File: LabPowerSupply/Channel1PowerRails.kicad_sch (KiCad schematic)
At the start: 8 parts

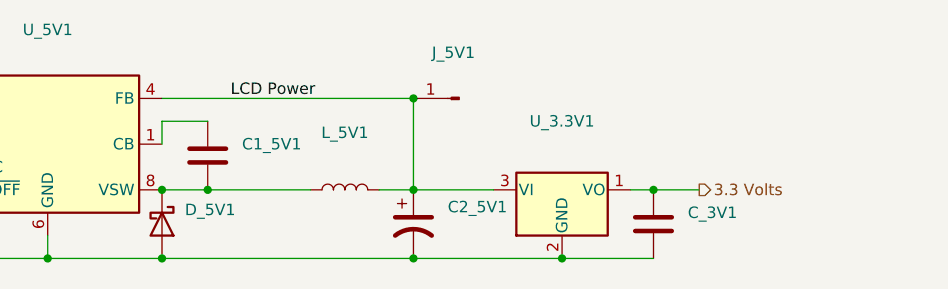
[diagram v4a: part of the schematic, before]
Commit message: Changed capacitor footprints, added resistor and diode to linear
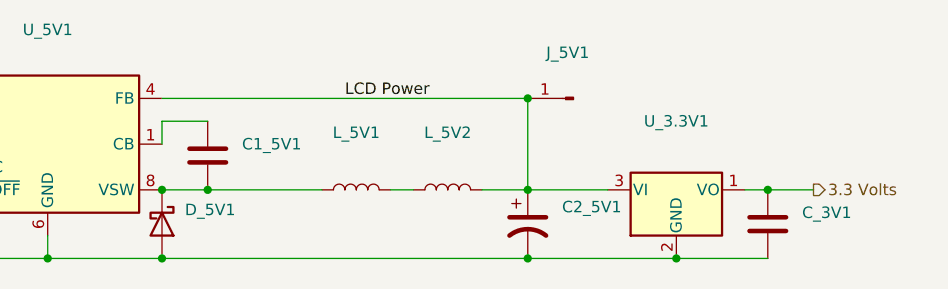
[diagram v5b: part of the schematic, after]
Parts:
- added L_5V1: (no value), symbol Device:L
- renumbered L_5V1 to L_5V2
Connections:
- net at C1_5V1.2, D_5V1.1 (K), U_5V1.8 (VSW): now also L_5V1.1; no longer L_5V2.1
- new net: L_5V1.2, L_5V2.1
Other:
- moved on the sheet: C2_5V1, C_3V1, J_5V1, L_5V2, U_3.3V1
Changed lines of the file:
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@@
   (junction (at 139.7 99.06) (diameter 0) (color 0 0 0 0)
+  )
+  (junction (at 144.78 99.06) (diameter 0) (color 0 0 0 0)
   )
   (junction (at 139.7 106.68) (diameter 0) (color 0 0 0 0)
   )
-  (junction (at 144.78 99.06) (diameter 0) (color 0 0 0 0)
+  (junction (at 180.34 99.06) (diameter 0) (color 0 0 0 0)
   )
-  (junction (at 167.64 99.06) (diameter 0) (color 0 0 0 0)
+  (junction (at 180.34 88.9) (diameter 0) (color 0 0 0 0)
   )
-  (junction (at 167.64 88.9) (diameter 0) (color 0 0 0 0)
+  (junction (at 207.01 99.06) (diameter 0) (color 0 0 0 0)
   )
-  (junction (at 194.31 99.06) (diameter 0) (color 0 0 0 0)
+  (junction (at 180.34 106.68) (diameter 0) (color 0 0 0 0)
   )
-  (junction (at 167.64 106.68) (diameter 0) (color 0 0 0 0)
-  )
-  (junction (at 184.15 106.68) (diameter 0) (color 0 0 0 0)
+  (junction (at 196.85 106.68) (diameter 0) (color 0 0 0 0)
   )
   (no_connect (at 114.3 96.52))
@@
     (stroke (width 0) (type default) (color 0 0 0 0))
   )
-  (wire (pts (xy 167.64 99.06) (xy 176.53 99.06))
+  (wire (pts (xy 180.34 99.06) (xy 189.23 99.06))
     (stroke (width 0) (type default) (color 0 0 0 0))
   )
@@
     (stroke (width 0) (type default) (color 0 0 0 0))
   )
-  (wire (pts (xy 156.21 99.06) (xy 144.78 99.06))
+  (wire (pts (xy 144.78 99.06) (xy 157.48 99.06))
+    (stroke (width 0) (type default) (color 0 0 0 0))
+  )
+  (wire (pts (xy 139.7 106.68) (xy 180.34 106.68))
     (stroke (width 0) (type default) (color 0 0 0 0))
   )
@@
     (stroke (width 0) (type default) (color 0 0 0 0))
   )
-  (wire (pts (xy 167.64 88.9) (xy 139.7 88.9))
+  (wire (pts (xy 139.7 88.9) (xy 180.34 88.9))
     (stroke (width 0) (type default) (color 0 0 0 0))
   )
-  (wire (pts (xy 167.64 106.68) (xy 184.15 106.68))
+  (wire (pts (xy 180.34 106.68) (xy 196.85 106.68))
     (stroke (width 0) (type default) (color 0 0 0 0))
   )
-  (wire (pts (xy 167.64 99.06) (xy 167.64 88.9))
+  (wire (pts (xy 180.34 99.06) (xy 180.34 88.9))
+    (stroke (width 0) (type default) (color 0 0 0 0))
+  )
+  (wire (pts (xy 165.1 99.06) (xy 167.64 99.06))
     (stroke (width 0) (type default) (color 0 0 0 0))
   )
@@
     (stroke (width 0) (type default) (color 0 0 0 0))
   )
-  (wire (pts (xy 139.7 106.68) (xy 167.64 106.68))
-    (stroke (width 0) (type default) (color 0 0 0 0))
-  )
   (wire (pts (xy 113.03 106.68) (xy 127 106.68))
     (stroke (width 0) (type default) (color 0 0 0 0))
   )
-  (wire (pts (xy 184.15 106.68) (xy 194.31 106.68))
+  (wire (pts (xy 196.85 106.68) (xy 207.01 106.68))
     (stroke (width 0) (type default) (color 0 0 0 0))
   )
-  (wire (pts (xy 194.31 99.06) (xy 199.39 99.06))
+  (wire (pts (xy 207.01 99.06) (xy 212.09 99.06))
     (stroke (width 0) (type default) (color 0 0 0 0))
   )
-  (wire (pts (xy 191.77 99.06) (xy 194.31 99.06))
+  (wire (pts (xy 204.47 99.06) (xy 207.01 99.06))
     (stroke (width 0) (type default) (color 0 0 0 0))
   )
-  (wire (pts (xy 163.83 99.06) (xy 167.64 99.06))
+  (wire (pts (xy 175.26 99.06) (xy 180.34 99.06))
     (stroke (width 0) (type default) (color 0 0 0 0))
   )
-  (label "LCD Power" (at 147.32 88.9 0)
+  (label "LCD Power" (at 160.02 88.9 0)
     (effects (font (size 1.27 1.27)) (justify left bottom))
   )
@@
     (effects (font (size 1.27 1.27)) (justify right))
   )
-  (hierarchical_label "3.3 Volts" (shape output) (at 199.39 99.06 0)
+  (hierarchical_label "3.3 Volts" (shape output) (at 212.09 99.06 0)
     (effects (font (size 1.27 1.27)) (justify left))
   )
@@
     (effects (font (size 1.27 1.27)) (justify right))
   )
-  (symbol (lib_id "Connector:Conn_01x01_Male") (at 172.72 88.9 180) (unit 1)
+  (symbol (lib_id "Connector:Conn_01x01_Male") (at 185.42 88.9 180) (unit 1)
     (in_bom yes) (on_board yes) (fields_autoplaced)
-    (property "Reference" "J_5V1" (id 0) (at 172.085 83.82 0))
-    (property "Value" "" (id 1) (at 172.085 86.36 0))
-    (property "Footprint" "" (id 2) (at 172.72 88.9 0)
+    (property "Reference" "J_5V1" (id 0) (at 184.785 83.82 0))
+    (property "Value" "" (id 1) (at 184.785 86.36 0))
+    (property "Footprint" "" (id 2) (at 185.42 88.9 0)
       (effects (font (size 1.27 1.27)) hide)
     )
-    (property "Datasheet" "~" (id 3) (at 172.72 88.9 0)
+    (property "Datasheet" "~" (id 3) (at 185.42 88.9 0)
       (effects (font (size 1.27 1.27)) hide)
     )
     (pin "1")
   )
-  (symbol (lib_id "Device:C") (at 194.31 102.87 0) (unit 1)
+  (symbol (lib_id "Device:C") (at 207.01 102.87 0) (unit 1)
     (in_bom yes) (on_board yes) (fields_autoplaced)
-    (property "Reference" "C_3V1" (id 0) (at 198.12 101.5999 0)
+    (property "Reference" "C_3V1" (id 0) (at 210.82 101.5999 0)
       (effects (font (size 1.27 1.27)) (justify left))
     )
-    (property "Value" "" (id 1) (at 198.12 104.1399 0)
+    (property "Value" "" (id 1) (at 210.82 104.1399 0)
       (effects (font (size 1.27 1.27)) (justify left))
     )
-    (property "Footprint" "" (id 2) (at 195.2752 106.68 0)
+    (property "Footprint" "" (id 2) (at 207.9752 106.68 0)
       (effects (font (size 1.27 1.27)) hide)
     )
-    (property "Datasheet" "~" (id 3) (at 194.31 102.87 0)
+    (property "Datasheet" "~" (id 3) (at 207.01 102.87 0)
       (effects (font (size 1.27 1.27)) hide)
     )
@@
     (pin "2")
   )
-  (symbol (lib_id "Regulator_Linear:LP2950-3.3_TO92") (at 184.15 99.06 0) (unit 1)
+  (symbol (lib_id "Regulator_Linear:LP2950-3.3_TO92") (at 196.85 99.06 0) (unit 1)
     (in_bom yes) (on_board yes) (fields_autoplaced)
-    (property "Reference" "U_3.3V1" (id 0) (at 184.15 91.44 0))
-    (property "Value" "" (id 1) (at 184.15 93.98 0))
-    (property "Footprint" "" (id 2) (at 184.15 93.345 0)
+    (property "Reference" "U_3.3V1" (id 0) (at 196.85 91.44 0))
+    (property "Value" "" (id 1) (at 196.85 93.98 0))
+    (property "Footprint" "" (id 2) (at 196.85 93.345 0)
       (effects (font (size 1.27 1.27) italic) hide)
     )
-    (property "Datasheet" "http://www.ti.com/lit/ds/symlink/lp2950.pdf" (id 3) (at 184.15 100.33 0)
+    (property "Datasheet" "http://www.ti.com/lit/ds/symlink/lp2950.pdf" (id 3) (at 196.85 100.33 0)
       (effects (font (size 1.27 1.27)) hide)
     )
@@
     (pin "3")
   )
-  (symbol (lib_id "Device:C_Polarized_US") (at 167.64 102.87 0) (unit 1)
+  (symbol (lib_id "Device:C_Polarized_US") (at 180.34 102.87 0) (unit 1)
     (in_bom yes) (on_board yes) (fields_autoplaced)
-    (property "Reference" "C2_5V1" (id 0) (at 171.45 100.9649 0)
+    (property "Reference" "C2_5V1" (id 0) (at 184.15 100.9649 0)
       (effects (font (size 1.27 1.27)) (justify left))
     )
-    (property "Value" "" (id 1) (at 171.45 103.5049 0)
+    (property "Value" "" (id 1) (at 184.15 103.5049 0)
       (effects (font (size 1.27 1.27)) (justify left))
     )
-    (property "Footprint" "" (id 2) (at 167.64 102.87 0)
+    (property "Footprint" "" (id 2) (at 180.34 102.87 0)
       (effects (font (size 1.27 1.27)) hide)
     )
-    (property "Datasheet" "~" (id 3) (at 167.64 102.87 0)
+    (property "Datasheet" "~" (id 3) (at 180.34 102.87 0)
       (effects (font (size 1.27 1.27)) hide)
     )
@@
     (pin "2")
   )
-  (symbol (lib_id "Device:L") (at 160.02 99.06 90) (unit 1)
+  (symbol (lib_id "Device:L") (at 161.29 99.06 90) (unit 1)
     (in_bom yes) (on_board yes) (fields_autoplaced)
-    (property "Reference" "L_5V1" (id 0) (at 160.02 92.71 90))
-    (property "Value" "" (id 1) (at 160.02 95.25 90))
-    (property "Footprint" "" (id 2) (at 160.02 99.06 0)
+    (property "Reference" "L_5V1" (id 0) (at 161.29 92.71 90))
+    (property "Value" "" (id 1) (at 161.29 95.25 90))
+    (property "Footprint" "" (id 2) (at 161.29 99.06 0)
       (effects (font (size 1.27 1.27)) hide)
     )
-    (property "Datasheet" "~" (id 3) (at 160.02 99.06 0)
+    (property "Datasheet" "~" (id 3) (at 161.29 99.06 0)
       (effects (font (size 1.27 1.27)) hide)
     )
+    (pin "1")
+    (pin "2")
+  )
+  (symbol (lib_id "Device:L") (at 171.45 99.06 90) (unit 1)
+    (in_bom yes) (on_board yes) (fields_autoplaced)
+    (property "Reference" "L_5V2" (id 0) (at 171.45 92.71 90))
+    (property "Value" "" (id 1) (at 171.45 95.25 90))
+    (property "Footprint" "" (id 2) (at 171.45 99.06 0)
+      (effects (font (size 1.27 1.27)) hide)
+    )
+    (property "Datasheet" "~" (id 3) (at 171.45 99.06 0)
+      (effects (font (size 1.27 1.27)) hide)
+    )

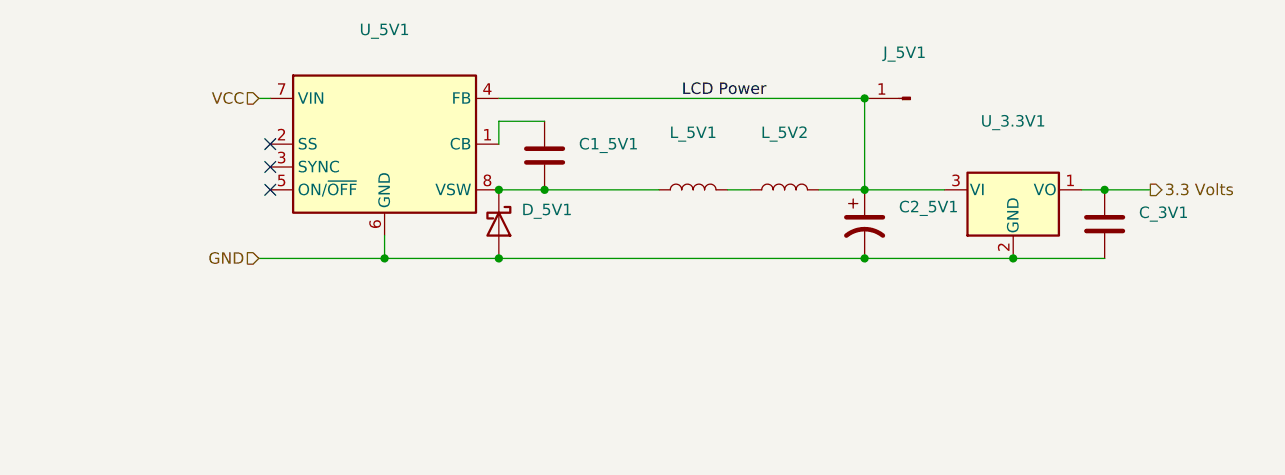
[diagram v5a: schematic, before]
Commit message: Added mcu capacitors, split 5v inductors
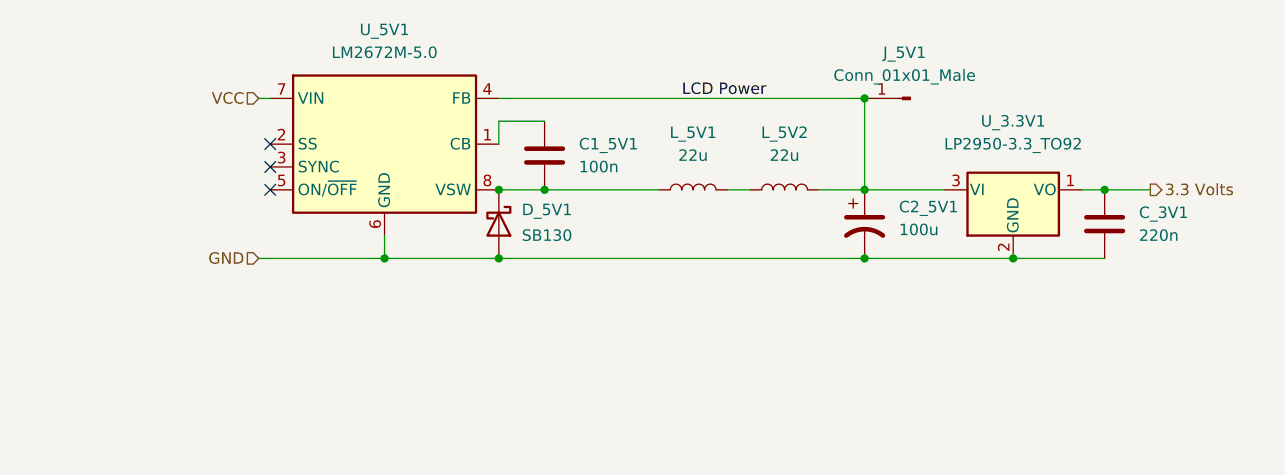
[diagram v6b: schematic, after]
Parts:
- C1_5V1: value (none) -> 100n; footprint (none) -> Capacitor_THT:C_Disc_D5.0mm_W2.5mm_P2.50mm
- C2_5V1: value (none) -> 100u; footprint (none) -> Capacitor_THT:CP_Radial_D10.0mm_P5.00mm
- C_3V1: value (none) -> 220n; footprint (none) -> Capacitor_THT:C_Disc_D5.0mm_W2.5mm_P2.50mm
- D_5V1: value (none) -> SB130; footprint (none) -> Diode_THT:D_DO-41_SOD81_P10.16mm_Horizontal
- J_5V1: value (none) -> Conn_01x01_Male; footprint (none) -> Connector_PinHeader_2.54mm:PinHeader_1x01_P2.54mm_Vertical
- L_5V1, L_5V2: value (none) -> 22u; footprint (none) -> Inductor_THT:L_Radial_D6.0mm_P4.00mm
- U_3.3V1: value (none) -> LP2950-3.3_TO92; footprint (none) -> Package_TO_SOT_THT:TO-92_Inline
- U_5V1: value (none) -> LM2672M-5.0; footprint (none) -> Package_SO:SOIC-8_3.9x4.9mm_P1.27mm
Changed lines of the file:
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@@
     (in_bom yes) (on_board yes) (fields_autoplaced)
     (property "Reference" "J_5V1" (id 0) (at 184.785 83.82 0))
-    (property "Value" "" (id 1) (at 184.785 86.36 0))
-    (property "Footprint" "" (id 2) (at 185.42 88.9 0)
+    (property "Value" "Conn_01x01_Male" (id 1) (at 184.785 86.36 0))
+    (property "Footprint" "Connector_PinHeader_2.54mm:PinHeader_1x01_P2.54mm_Vertical" (id 2) (at 185.42 88.9 0)
       (effects (font (size 1.27 1.27)) hide)
     )
@@
       (effects (font (size 1.27 1.27)) (justify left))
     )
-    (property "Value" "" (id 1) (at 210.82 104.1399 0)
+    (property "Value" "220n" (id 1) (at 210.82 104.1399 0)
       (effects (font (size 1.27 1.27)) (justify left))
     )
-    (property "Footprint" "" (id 2) (at 207.9752 106.68 0)
+    (property "Footprint" "Capacitor_THT:C_Disc_D5.0mm_W2.5mm_P2.50mm" (id 2) (at 207.9752 106.68 0)
       (effects (font (size 1.27 1.27)) hide)
     )
@@
     (in_bom yes) (on_board yes) (fields_autoplaced)
     (property "Reference" "U_3.3V1" (id 0) (at 196.85 91.44 0))
-    (property "Value" "" (id 1) (at 196.85 93.98 0))
-    (property "Footprint" "" (id 2) (at 196.85 93.345 0)
+    (property "Value" "LP2950-3.3_TO92" (id 1) (at 196.85 93.98 0))
+    (property "Footprint" "Package_TO_SOT_THT:TO-92_Inline" (id 2) (at 196.85 93.345 0)
       (effects (font (size 1.27 1.27) italic) hide)
     )
@@
       (effects (font (size 1.27 1.27)) (justify left))
     )
-    (property "Value" "" (id 1) (at 184.15 103.5049 0)
+    (property "Value" "100u" (id 1) (at 184.15 103.5049 0)
       (effects (font (size 1.27 1.27)) (justify left))
     )
-    (property "Footprint" "" (id 2) (at 180.34 102.87 0)
+    (property "Footprint" "Capacitor_THT:CP_Radial_D10.0mm_P5.00mm" (id 2) (at 180.34 102.87 0)
       (effects (font (size 1.27 1.27)) hide)
     )
@@
       (effects (font (size 1.27 1.27)) (justify left))
     )
-    (property "Value" "" (id 1) (at 142.24 104.14 90)
+    (property "Value" "SB130" (id 1) (at 142.24 104.14 90)
       (effects (font (size 1.27 1.27)) (justify left))
     )
-    (property "Footprint" "" (id 2) (at 135.255 102.87 0)
+    (property "Footprint" "Diode_THT:D_DO-41_SOD81_P10.16mm_Horizontal" (id 2) (at 135.255 102.87 0)
       (effects (font (size 1.27 1.27)) hide)
     )
@@
     (in_bom yes) (on_board yes) (fields_autoplaced)
     (property "Reference" "L_5V1" (id 0) (at 161.29 92.71 90))
-    (property "Value" "" (id 1) (at 161.29 95.25 90))
-    (property "Footprint" "" (id 2) (at 161.29 99.06 0)
+    (property "Value" "22u" (id 1) (at 161.29 95.25 90))
+    (property "Footprint" "Inductor_THT:L_Radial_D6.0mm_P4.00mm" (id 2) (at 161.29 99.06 0)
       (effects (font (size 1.27 1.27)) hide)
     )
@@
     (in_bom yes) (on_board yes) (fields_autoplaced)
     (property "Reference" "L_5V2" (id 0) (at 171.45 92.71 90))
-    (property "Value" "" (id 1) (at 171.45 95.25 90))
-    (property "Footprint" "" (id 2) (at 171.45 99.06 0)
+    (property "Value" "22u" (id 1) (at 171.45 95.25 90))
+    (property "Footprint" "Inductor_THT:L_Radial_D6.0mm_P4.00mm" (id 2) (at 171.45 99.06 0)
       (effects (font (size 1.27 1.27)) hide)
     )
@@
     (in_bom yes) (on_board yes) (fields_autoplaced)
     (property "Reference" "U_5V1" (id 0) (at 127 81.28 0))
-    (property "Value" "" (id 1) (at 127 83.82 0))
-    (property "Footprint" "" (id 2) (at 128.27 102.87 0)
+    (property "Value" "LM2672M-5.0" (id 1) (at 127 83.82 0))
+    (property "Footprint" "Package_SO:SOIC-8_3.9x4.9mm_P1.27mm" (id 2) (at 128.27 102.87 0)
       (effects (font (size 1.27 1.27) italic) (justify left) hide)
     )
@@
       (effects (font (size 1.27 1.27)) (justify left))
     )
-    (property "Value" "" (id 1) (at 148.59 96.5199 0)
+    (property "Value" "100n" (id 1) (at 148.59 96.5199 0)
       (effects (font (size 1.27 1.27)) (justify left))
     )
-    (property "Footprint" "" (id 2) (at 145.7452 99.06 0)
+    (property "Footprint" "Capacitor_THT:C_Disc_D5.0mm_W2.5mm_P2.50mm" (id 2) (at 145.7452 99.06 0)
       (effects (font (size 1.27 1.27)) hide)
     )

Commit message: Fixed 5v/3v regulators, fixed switching regulator comp
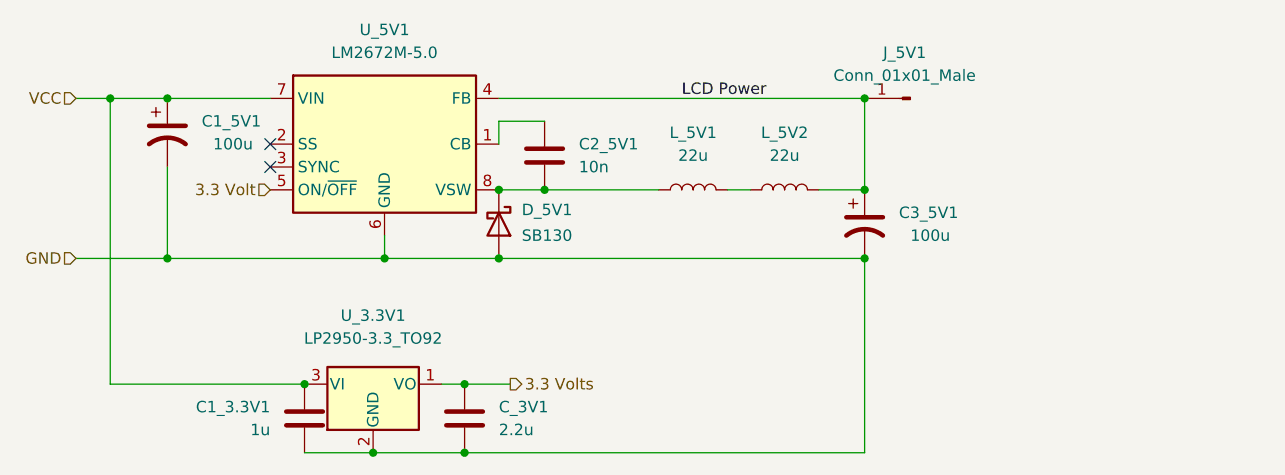
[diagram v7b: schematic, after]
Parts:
- added C1_3.3V1: 1u, Capacitor_THT:C_Disc_D5.0mm_W2.5mm_P2.50mm, symbol Device:C
- added C1_5V1: 100u, Capacitor_THT:CP_Radial_D10.0mm_P5.00mm, symbol Device:C_Polarized_US
- C2_5V1: renamed from C1_5V1; value 100n -> 10n; footprint Capacitor_THT:C_Disc_D5.0mm_W2.5mm_P2.50mm -> Capacitor_THT:C_Disc_D6.0mm_W2.5mm_P5.00mm
- C_3V1: value 220n -> 2.2u
- renumbered C2_5V1 to C3_5V1
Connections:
- net GND: now also C1_3.3V1.1, C1_5V1.2
- net LCD Power: no longer U_3.3V1.3 (VI)
- net VCC: now also U_3.3V1.3 (VI), C1_3.3V1.2, C1_5V1.1
- net 3.3 Volt: now reaches U_5V1.5 (ON/~{OFF})
- no-connect marks 3 -> 2
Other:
- moved on the sheet: C_3V1, U_3.3V1
